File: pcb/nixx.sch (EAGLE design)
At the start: 43 parts, among them IC1 24C64ST

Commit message: started firmware
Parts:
- added R21: (no value), joyAnalog:RESISTOR0805-RES
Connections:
- net GND: now also R21.1
- net STM_DOT_RIGHT: now also R21.2
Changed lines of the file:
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@@
 <part name="+3V9" library="joyAnalog" deviceset="+3V3" device=""/>
 <part name="TP1" library="testpad" deviceset="PTR1" device="TP13R" value="PTR1TP13R"/>
+<part name="R21" library="joyAnalog" deviceset="RESISTOR" device="0805-RES"/>
+<part name="GND17" library="joyAnalog" deviceset="GND" device=""/>
 </parts>
 <sheets>
@@
 <instance part="+3V9" gate="G$1" x="284.48" y="71.12"/>
 <instance part="TP1" gate="G$1" x="365.76" y="63.5" rot="R90"/>
+<instance part="R21" gate="G$1" x="347.98" y="27.94" rot="R90"/>
+<instance part="GND17" gate="1" x="347.98" y="20.32"/>
 </instances>
 <busses>
@@
 <junction x="284.48" y="38.1"/>
 </segment>
+<segment>
+<pinref part="R21" gate="G$1" pin="1"/>
+<pinref part="GND17" gate="1" pin="GND"/>
+</segment>
 </net>
 <net name="N$1" class="0">
@@
 </segment>
 <segment>
-<wire x1="355.6" y1="33.02" x2="340.36" y2="33.02" width="0.1524" layer="91"/>
+<wire x1="355.6" y1="33.02" x2="347.98" y2="33.02" width="0.1524" layer="91"/>
 <pinref part="U$2" gate="G$1" pin="PB8"/>
 <label x="342.9" y="33.02" size="1.778" layer="95"/>
-</segment>
-</net>
+<pinref part="R21" gate="G$1" pin="2"/>
+<wire x1="347.98" y1="33.02" x2="340.36" y2="33.02" width="0.1524" layer="91"/>
+<junction x="347.98" y="33.02"/>
+</segment>
+</net>

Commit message: added pulldown on BOOT0
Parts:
- C1: value (none) -> 1uF
- C2, C3, C4: value (none) -> 100nF
- R1, R10, R11, R12, R17, R18, R19, R2, R20, R3, R4, R5, R6, R7, R8, R9: value (none) -> 4K7
- R13, R21: value (none) -> 10K
- R14, R15: value (none) -> 470
- R16: value (none) -> 0
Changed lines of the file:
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@@
 <part name="P+2" library="nixx" deviceset="+180V" device=""/>
 <part name="P+1" library="nixx" deviceset="+180V" device=""/>
-<part name="R1" library="joyAnalog" deviceset="RESISTOR" device="0805-RES"/>
-<part name="C1" library="joyAnalog" deviceset="CAP" device="0805"/>
+<part name="R1" library="joyAnalog" deviceset="RESISTOR" device="0805-RES" value="4K7"/>
+<part name="C1" library="joyAnalog" deviceset="CAP" device="0805" value="1uF"/>
 <part name="GND1" library="joyAnalog" deviceset="GND" device=""/>
 <part name="Q2" library="nixx" deviceset="BF820" device=""/>
-<part name="R2" library="joyAnalog" deviceset="RESISTOR" device="0805-RES"/>
+<part name="R2" library="joyAnalog" deviceset="RESISTOR" device="0805-RES" value="4K7"/>
 <part name="GND2" library="joyAnalog" deviceset="GND" device=""/>
 <part name="Q3" library="nixx" deviceset="BF820" device=""/>
-<part name="R3" library="joyAnalog" deviceset="RESISTOR" device="0805-RES"/>
+<part name="R3" library="joyAnalog" deviceset="RESISTOR" device="0805-RES" value="4K7"/>
 <part name="GND3" library="joyAnalog" deviceset="GND" device=""/>
 <part name="Q4" library="nixx" deviceset="BF820" device=""/>
-<part name="R4" library="joyAnalog" deviceset="RESISTOR" device="0805-RES"/>
+<part name="R4" library="joyAnalog" deviceset="RESISTOR" device="0805-RES" value="4K7"/>
 <part name="GND4" library="joyAnalog" deviceset="GND" device=""/>
 <part name="Q5" library="nixx" deviceset="BF820" device=""/>
-<part name="R5" library="joyAnalog" deviceset="RESISTOR" device="0805-RES"/>
+<part name="R5" library="joyAnalog" deviceset="RESISTOR" device="0805-RES" value="4K7"/>
 <part name="GND5" library="joyAnalog" deviceset="GND" device=""/>
 <part name="Q6" library="nixx" deviceset="BF820" device=""/>
-<part name="R6" library="joyAnalog" deviceset="RESISTOR" device="0805-RES"/>
+<part name="R6" library="joyAnalog" deviceset="RESISTOR" device="0805-RES" value="4K7"/>
 <part name="GND6" library="joyAnalog" deviceset="GND" device=""/>
 <part name="Q7" library="nixx" deviceset="BF820" device=""/>
-<part name="R7" library="joyAnalog" deviceset="RESISTOR" device="0805-RES"/>
+<part name="R7" library="joyAnalog" deviceset="RESISTOR" device="0805-RES" value="4K7"/>
 <part name="GND7" library="joyAnalog" deviceset="GND" device=""/>
 <part name="Q8" library="nixx" deviceset="BF820" device=""/>
-<part name="R8" library="joyAnalog" deviceset="RESISTOR" device="0805-RES"/>
+<part name="R8" library="joyAnalog" deviceset="RESISTOR" device="0805-RES" value="4K7"/>
 <part name="GND8" library="joyAnalog" deviceset="GND" device=""/>
 <part name="Q9" library="nixx" deviceset="BF820" device=""/>
-<part name="R9" library="joyAnalog" deviceset="RESISTOR" device="0805-RES"/>
+<part name="R9" library="joyAnalog" deviceset="RESISTOR" device="0805-RES" value="4K7"/>
 <part name="GND9" library="joyAnalog" deviceset="GND" device=""/>
 <part name="Q10" library="nixx" deviceset="BF820" device=""/>
-<part name="R10" library="joyAnalog" deviceset="RESISTOR" device="0805-RES"/>
+<part name="R10" library="joyAnalog" deviceset="RESISTOR" device="0805-RES" value="4K7"/>
 <part name="GND10" library="joyAnalog" deviceset="GND" device=""/>
 <part name="Q11" library="nixx" deviceset="BF820" device=""/>
-<part name="R11" library="joyAnalog" deviceset="RESISTOR" device="0805-RES"/>
+<part name="R11" library="joyAnalog" deviceset="RESISTOR" device="0805-RES" value="4K7"/>
 <part name="GND11" library="joyAnalog" deviceset="GND" device=""/>
 <part name="Q12" library="nixx" deviceset="BF820" device=""/>
-<part name="R12" library="joyAnalog" deviceset="RESISTOR" device="0805-RES"/>
+<part name="R12" library="joyAnalog" deviceset="RESISTOR" device="0805-RES" value="4K7"/>
 <part name="GND12" library="joyAnalog" deviceset="GND" device=""/>
 <part name="GND13" library="joyAnalog" deviceset="GND" device=""/>
 <part name="+3V1" library="joyAnalog" deviceset="+3V3" device=""/>
-<part name="C2" library="joyAnalog" deviceset="CAP" device="0805"/>
-<part name="C3" library="joyAnalog" deviceset="CAP" device="0805"/>
+<part name="C2" library="joyAnalog" deviceset="CAP" device="0805" value="100nF"/>
+<part name="C3" library="joyAnalog" deviceset="CAP" device="0805" value="100nF"/>
 <part name="GND14" library="joyAnalog" deviceset="GND" device=""/>
 <part name="+3V2" library="joyAnalog" deviceset="+3V3" device=""/>
@@
 <part name="+3V3" library="joyAnalog" deviceset="+3V3" device=""/>
 <part name="D1" library="nixx" deviceset="RGB_LED_CA" device="-150141M173100-R&amp;G&amp;B"/>
-<part name="R13" library="joyAnalog" deviceset="RESISTOR" device="0805-RES"/>
+<part name="R13" library="joyAnalog" deviceset="RESISTOR" device="0805-RES" value="10K"/>
 <part name="+3V4" library="joyAnalog" deviceset="+3V3" device=""/>
-<part name="R14" library="joyAnalog" deviceset="RESISTOR" device="0805-RES"/>
-<part name="R15" library="joyAnalog" deviceset="RESISTOR" device="0805-RES"/>
-<part name="R16" library="joyAnalog" deviceset="RESISTOR" device="0805-RES"/>
-<part name="R17" library="joyAnalog" deviceset="RESISTOR" device="0805-RES"/>
-<part name="R18" library="joyAnalog" deviceset="RESISTOR" device="0805-RES"/>
+<part name="R14" library="joyAnalog" deviceset="RESISTOR" device="0805-RES" value="470"/>
+<part name="R15" library="joyAnalog" deviceset="RESISTOR" device="0805-RES" value="470"/>
+<part name="R16" library="joyAnalog" deviceset="RESISTOR" device="0805-RES" value="0"/>
+<part name="R17" library="joyAnalog" deviceset="RESISTOR" device="0805-RES" value="4K7"/>
+<part name="R18" library="joyAnalog" deviceset="RESISTOR" device="0805-RES" value="4K7"/>
 <part name="+3V5" library="joyAnalog" deviceset="+3V3" device=""/>
 <part name="+3V6" library="joyAnalog" deviceset="+3V3" device=""/>
-<part name="C4" library="joyAnalog" deviceset="CAP" device="0805"/>
+<part name="C4" library="joyAnalog" deviceset="CAP" device="0805" value="100nF"/>
 <part name="IC1" library="joyAnalog" deviceset="24*" device="ST" technology="C64"/>
-<part name="R19" library="joyAnalog" deviceset="RESISTOR" device="0805-RES"/>
-<part name="R20" library="joyAnalog" deviceset="RESISTOR" device="0805-RES"/>
+<part name="R19" library="joyAnalog" deviceset="RESISTOR" device="0805-RES" value="4K7"/>
+<part name="R20" library="joyAnalog" deviceset="RESISTOR" device="0805-RES" value="4K7"/>
 <part name="+3V7" library="joyAnalog" deviceset="+3V3" device=""/>
 <part name="+3V8" library="joyAnalog" deviceset="+3V3" device=""/>
@@
 <part name="+3V9" library="joyAnalog" deviceset="+3V3" device=""/>
 <part name="TP1" library="testpad" deviceset="PTR1" device="TP13R" value="PTR1TP13R"/>
-<part name="R21" library="joyAnalog" deviceset="RESISTOR" device="0805-RES"/>
+<part name="R21" library="joyAnalog" deviceset="RESISTOR" device="0805-RES" value="10K"/>
 <part name="GND17" library="joyAnalog" deviceset="GND" device=""/>
 </parts>

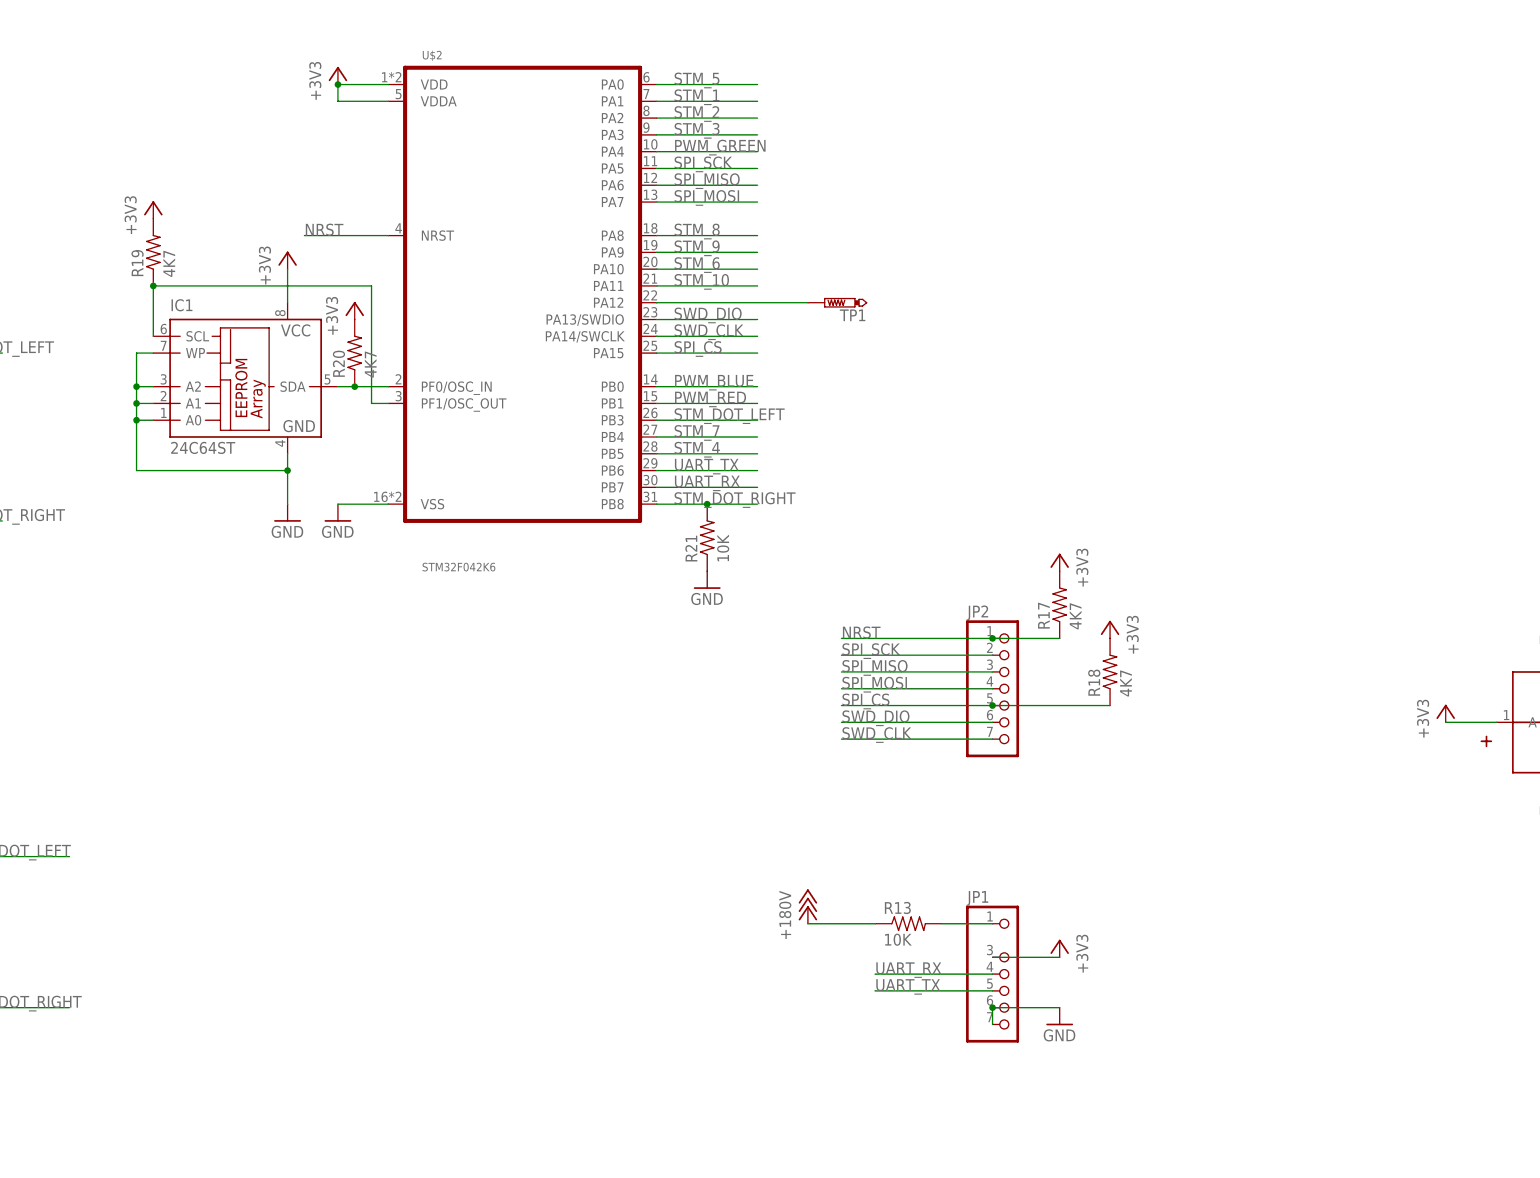
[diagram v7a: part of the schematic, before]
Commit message: made eeprom optional, added PF silkscreen
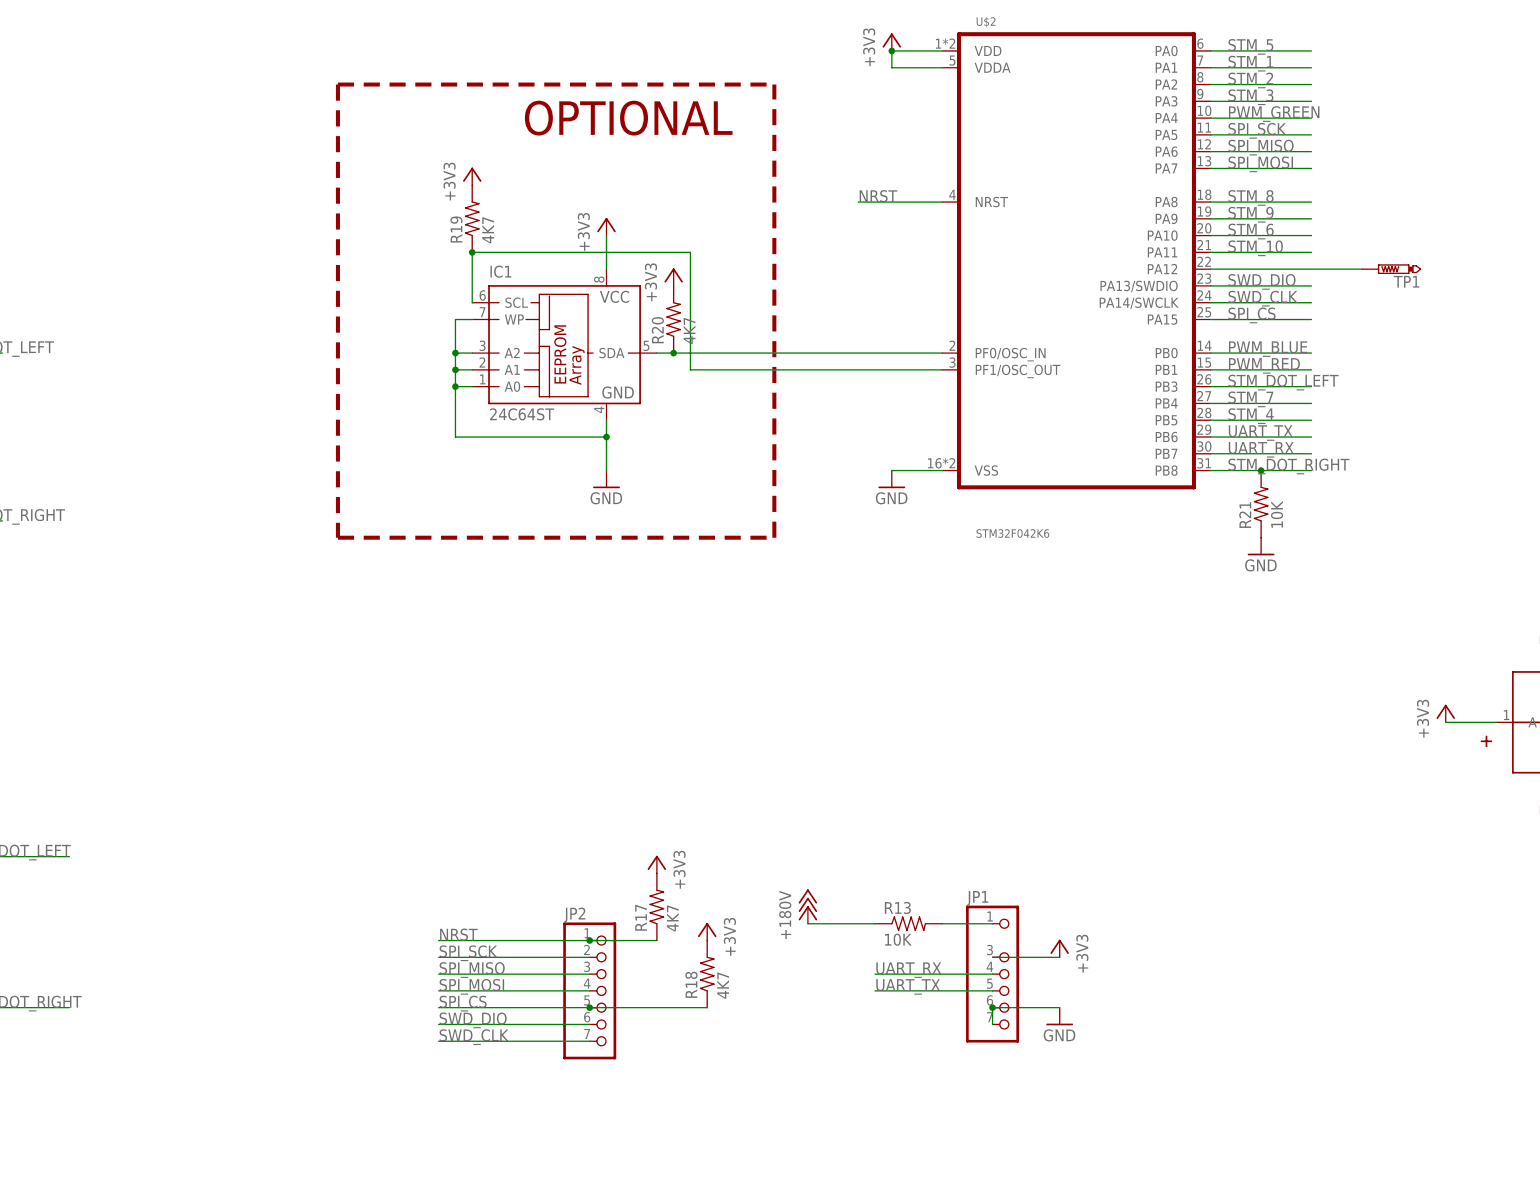
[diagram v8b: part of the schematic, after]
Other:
- note added: "OPTIONAL"
- moved on the sheet: IC1, JP2, R17, R18, R19, R20, R21, TP1, U$2
